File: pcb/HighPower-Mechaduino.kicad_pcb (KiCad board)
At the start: 2 copper layers, 60 x 60 mm, 124 parts, among them J1 SUPPLY, J2 STEPPER, P1 SWD, P2 USB, P3 PoStep25-32, P4 -, P5 -, P6 -, P7 -, Q1 SSM3J328R, Q10 IPD220N06L3, Q11 BSS138, Q2 BSS138, Q3 IPD220N06L3, Q4 IPD220N06L3, Q5 IPD220N06L3, Q6 IPD220N06L3, Q7 IPD220N06L3, Q8 IPD220N06L3, Q9 IPD220N06L3, SW1 SW_PUSH, U1 AS5047D, U2 AP2112K-3.3TRG1, U3 AT24CS64-SSHM, U4 SAMD21G18A-A, U5 A4955GLPTR-T, U6 A4955GLPTR-T, U7 USBLC6-2SC6, U8 MCP16331T, Y1 32.768kHz

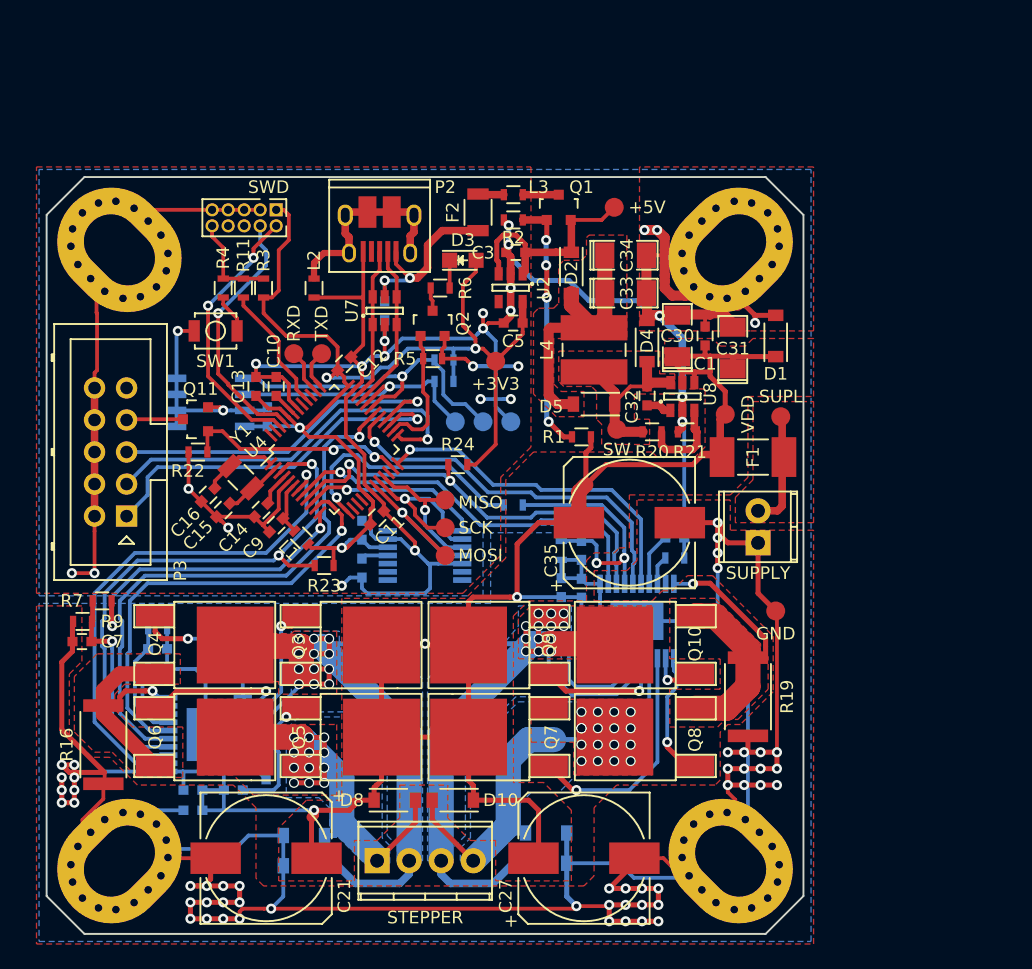
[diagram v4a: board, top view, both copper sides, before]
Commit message: Improve layout and add voltage sensing circuit to layout
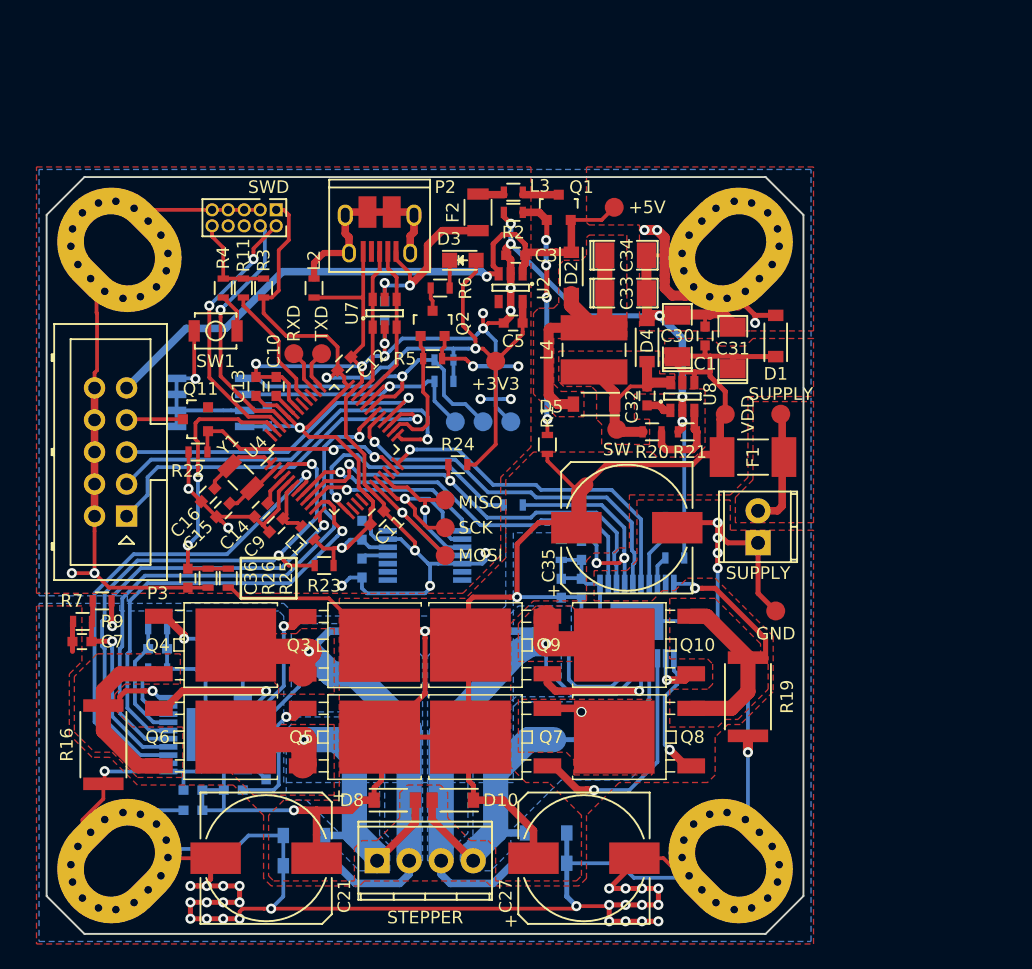
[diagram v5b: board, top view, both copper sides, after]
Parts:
- removed REF***: KiCad-Logo2_8mm_SilkScreen, Symbols:KiCad-Logo2_8mm_SilkScreen
- removed REF***: OSHW-Logo_11.4x12mm_SilkScreen, Symbols:OSHW-Logo_11.4x12mm_SilkScreen
- added C36: 100n, Capacitors_SMD:C_0603, F.Cu at (131.2, 101.8)
- added R25: 22k, Resistors_SMD:R_0603, F.Cu at (134.4, 101.8)
- added R26: 1k, Resistors_SMD:R_0603, F.Cu at (132.8, 101.8)
- Q10, Q3, Q4, Q5, Q6, Q7, Q8, Q9: footprint TO_SOT_Packages_SMD:TO-252-2Lead -> TO_SOT_Packages_SMD_local:PG-TO-252-3-313
- SW1: value SW_PUSH -> B3U-1000P
- W1: value SUPL -> SUPPLY
- Y1: value 32.768kHz -> G83270022
- moved Q10 3.35 mm to (168.1, 107.1)
- moved Q4 3.35 mm to (131.9, 107.1)
- moved Q6 3.35 mm to (131.9, 114.4)
- moved Q8 3.35 mm to (168.1, 114.4)
- moved Q3 3.15 mm to (143.3, 107.1)
- moved Q5 3.15 mm to (143.3, 114.4)
- moved Q7 3.15 mm to (156.7, 114.4)
- moved Q9 3.15 mm to (156.7, 107.1)
- moved R1 2.77 mm to (159.7, 91.2), turned to 270 degrees
- moved D12 1.00 mm to (153.4, 106.0)
- moved D6 1.00 mm to (146.6, 106.0)
- moved L1 0.64 mm to (140.7, 98.2)
- moved R2 0.60 mm to (157.0, 72.8)
- moved C35 0.45 mm to (166.0, 97.8)
- moved C3 0.23 mm to (157.2, 76.2)
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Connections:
- P3 pad 9: Net-(P3-Pad9) -> +5V
- U4 pad 47: /Arduino_Zero_Base/Arduino_A5 -> /A_IN
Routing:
- net GND: track 548.4 -> 505.9 mm, vias 78 -> 61
- net +5V: track 18.1 -> 51.8 mm, vias 0 -> 1
- net /A_IN: track 0.00 -> 22.0 mm, vias 0 -> 2
- net VDD: track 150.7 -> 166.7 mm
- net /PWM_Bridge_A4955-B/OUT2: track 51.7 -> 38.3 mm, vias 17 -> 1
- net /PWM_Bridge_A4955-A/OUT1: track 46.1 -> 34.5 mm, vias 12 -> 1
- net /PWM_Bridge_A4955-B/OUT1: track 70.1 -> 59.1 mm, vias 13 -> 1
- net /PWM_Bridge_A4955-A/OUT2: track 61.3 -> 54.8 mm, vias 12 -> 1
- net /Protected_USB_Supply/VBUS: track 0.00 -> 2.85 mm
- net Net-(F2-Pad1): track 4.92 -> 2.07 mm
- net /AIOUT1: track 41.4 -> 39.6 mm
- net Net-(Q10-Pad3): track 25.4 -> 23.8 mm
- net Net-(Q4-Pad3): track 18.4 -> 19.8 mm
- net /STP_STEP: track 28.0 -> 26.9 mm
- net Net-(Q1-Pad1): track 20.4 -> 19.3 mm
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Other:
- rule trace_min: 0.2 -> 0.3

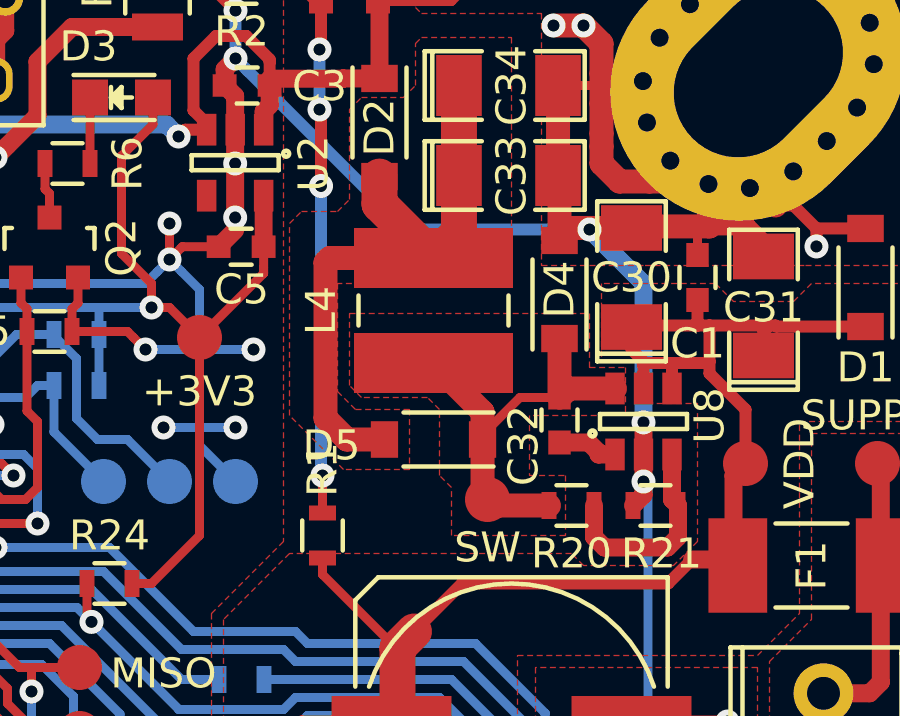
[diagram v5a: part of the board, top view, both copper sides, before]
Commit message: Fix inductor (old one was no longer available)
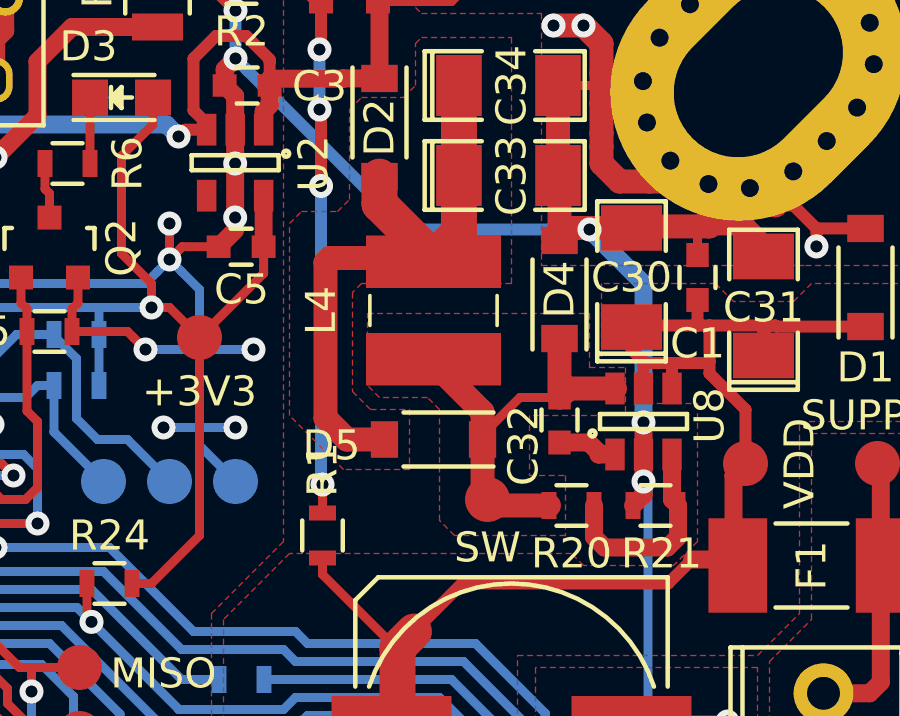
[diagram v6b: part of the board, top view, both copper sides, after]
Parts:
- L4: footprint Inductors_local:Inductor_Würth_SPC_4818 -> Inductors_local:Inductor_Würth_WE-PD2_4532
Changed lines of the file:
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@@
     (add_net /PWM_Bridge_A4955-B/OUT2)
   )
+  (module Inductors_local:Inductor_Würth_WE-PD2_4532 (layer F.Cu)
+    (at 163.4 83.7 90)
+    (descr "WE-PD2 SMD Power Inductor")
+    (tags "inductor würth")
+    (zone_connect 2)
+    (attr smd)
+    (fp_text reference L4 (at 0 -3.75 90) (layer F.SilkS)
+      (effects (font (size 1 1) (thickness 0.15)))
+    )
+    (fp_text value 22µ (at 0 0 180) (layer F.Fab)
+      (effects (font (size 1 1) (thickness 0.15)))
+    )
+    (fp_circle (center -1.8 0) (end -1.6 0) (layer F.Fab) (width 0.1))
+    (fp_arc (start 0 0) (end -1 2) (angle 126.8) (layer F.Fab) (width 0.1))
+    (fp_arc (start 0 0) (end 1 -2) (angle 126.8) (layer F.Fab) (width 0.1))
+    (fp_line (start -3 2.9) (end -3 -2.9) (layer F.CrtYd) (width 0.05))
+    (fp_line (start 3 2.9) (end -3 2.9) (layer F.CrtYd) (width 0.05))
+    (fp_line (start 3 -2.9) (end 3 2.9) (layer F.CrtYd) (width 0.05))
+    (fp_line (start -3 -2.9) (end 3 -2.9) (layer F.CrtYd) (width 0.05))
+    (fp_line (start -0.5 2.12) (end 0.5 2.12) (layer F.SilkS) (width 0.12))
+    (fp_line (start -0.5 -2.12) (end 0.5 -2.12) (layer F.SilkS) (width 0.12))
+    (fp_line (start 1 2) (end -1 2) (layer F.Fab) (width 0.1))
+    (fp_line (start -1 -2) (end 1 -2) (layer F.Fab) (width 0.1))
+    (pad 2 smd rect (at 1.625 0 90) (size 1.75 4.5) (layers F.Cu F.Paste F.Mask)
+      (net 22 /MCP16331_5V/VOUT) (zone_connect 2))
+    (pad 1 smd rect (at -1.625 0 90) (size 1.75 4.5) (layers F.Cu F.Paste F.Mask)
+      (net 21 "Net-(C32-Pad2)") (zone_connect 2))
+  )
   (module Measurement_Points:Measurement_Point_Round-SMD-Pad_Small (layer F.Cu)
     (at 177.8 104.4 180)
@@
       (effects (font (size 1 1) (thickness 0.15)))
     )
-    (fp_text value AP2112K-3.3TRG1 (at -0.05 1.988278 450) (layer F.Fab)
+    (fp_text value AP2112K-3.3TRG1 (at -0.05 1.988278 90) (layer F.Fab)
       (effects (font (size 1 1) (thickness 0.15)))
     )
@@
     )
   )
-  (module Inductors_local:Inductor_Würth_SPC_4818 (layer F.Cu)
-    (at 163.4 83.7 90)
-    (descr "WE-SPC SMD Shielded Power Inductor")
-    (tags "inductor würth")
-    (attr smd)
-    (fp_text reference L4 (at 0 -3.75 90) (layer F.SilkS)
-      (effects (font (size 1 1) (thickness 0.15)))
-    )
-    (fp_text value 22µ (at 0.1 0 180) (layer F.Fab)
-      (effects (font (size 1 1) (thickness 0.15)))
-    )
-    (fp_line (start -3 2.9) (end -3 -2.9) (layer F.CrtYd) (width 0.05))
-    (fp_line (start 3 2.9) (end -3 2.9) (layer F.CrtYd) (width 0.05))
-    (fp_line (start 3 -2.9) (end 3 2.9) (layer F.CrtYd) (width 0.05))
-    (fp_line (start -3 -2.9) (end 3 -2.9) (layer F.CrtYd) (width 0.05))
-    (fp_line (start -0.5 2.5) (end 0.5 2.5) (layer F.SilkS) (width 0.15))
-    (fp_line (start -0.5 -2.5) (end 0.5 -2.5) (layer F.SilkS) (width 0.15))
-    (fp_line (start -2.4 2.4) (end -2.4 -2.4) (layer F.Fab) (width 0.1))
-    (fp_line (start 2.4 2.4) (end -2.4 2.4) (layer F.Fab) (width 0.1))
-    (fp_line (start 2.4 -2.4) (end 2.4 2.4) (layer F.Fab) (width 0.1))
-    (fp_line (start -2.4 -2.4) (end 2.4 -2.4) (layer F.Fab) (width 0.1))
-    (pad 1 smd rect (at -1.75 0 90) (size 2 5.3) (layers F.Cu F.Paste F.Mask)
-      (net 21 "Net-(C32-Pad2)"))
-    (pad 2 smd rect (at 1.75 0 90) (size 2 5.3) (layers F.Cu F.Paste F.Mask)
-      (net 22 /MCP16331_5V/VOUT))
-  )
   (module Pin_Headers:Pin_Header_Straight_2x05_Pitch1.27mm (layer F.Cu)
     (at 138.2 72.6 270)
@@
     (tags "dpak TO-252 PG-TO-252")
     (attr smd)
-    (fp_text reference Q3 (at 0 3.35 360) (layer F.SilkS)
+    (fp_text reference Q3 (at 0 3.35) (layer F.SilkS)
       (effects (font (size 1 1) (thickness 0.15)))
     )
-    (fp_text value IPD220N06L3 (at 0.08 -1.05 360) (layer F.Fab)
+    (fp_text value IPD220N06L3 (at 0.08 -1.05) (layer F.Fab)
       (effects (font (size 1 1) (thickness 0.15)))
     )
@@
     (tags "dpak TO-252 PG-TO-252")
     (attr smd)
-    (fp_text reference Q4 (at 0 3.15 360) (layer F.SilkS)
+    (fp_text reference Q4 (at 0 3.15) (layer F.SilkS)
       (effects (font (size 1 1) (thickness 0.15)))
     )
-    (fp_text value IPD220N06L3 (at 0.1 -1.05 360) (layer F.Fab)
+    (fp_text value IPD220N06L3 (at 0.1 -1.05) (layer F.Fab)
       (effects (font (size 1 1) (thickness 0.15)))
     )
@@
     (tags "dpak TO-252 PG-TO-252")
     (attr smd)
-    (fp_text reference Q5 (at 0 3.15 360) (layer F.SilkS)
+    (fp_text reference Q5 (at 0 3.15) (layer F.SilkS)
       (effects (font (size 1 1) (thickness 0.15)))
     )
-    (fp_text value IPD220N06L3 (at 0 -1.05 540) (layer F.Fab)
+    (fp_text value IPD220N06L3 (at 0 -1.05 180) (layer F.Fab)
       (effects (font (size 1 1) (thickness 0.15)))
     )
@@
     (tags "dpak TO-252 PG-TO-252")
     (attr smd)
-    (fp_text reference Q6 (at 0 3.15 360) (layer F.SilkS)
+    (fp_text reference Q6 (at 0 3.15) (layer F.SilkS)
       (effects (font (size 1 1) (thickness 0.15)))
     )
-    (fp_text value IPD220N06L3 (at 0 -1.05 360) (layer F.Fab)
+    (fp_text value IPD220N06L3 (at 0 -1.05) (layer F.Fab)
       (effects (font (size 1 1) (thickness 0.15)))
     )
@@
   (segment (start 145.85 86.075127) (end 145.168807 86.75632) (width 0.3) (layer F.Cu) (net 36))
   (segment (start 145.168807 86.75632) (end 144.638478 87.286649) (width 0.3) (layer F.Cu) (net 36))
-  (segment (start 159.7 90.45) (end 159.7 89.2) (width 0.3) (layer F.Cu) (net 38))
-  (via (at 159.7 89.2) (size 0.8) (drill 0.4) (layers F.Cu B.Cu) (net 38))
-  (segment (start 159.65 79.55) (end 159.65 89.15) (width 0.4) (layer B.Cu) (net 38))
-  (segment (start 159.65 89.15) (end 159.7 89.2) (width 0.4) (layer B.Cu) (net 38))
+  (segment (start 159.65 89.45) (end 159.7 89.5) (width 0.4) (layer B.Cu) (net 38))
+  (segment (start 159.65 79.55) (end 159.65 89.45) (width 0.4) (layer B.Cu) (net 38))
+  (segment (start 159.7 90.45) (end 159.7 89.5) (width 0.3) (layer F.Cu) (net 38))
+  (via (at 159.7 89.5) (size 0.8) (drill 0.4) (layers F.Cu B.Cu) (net 38))
   (segment (start 157.75 72.8) (end 159.04924 72.8) (width 0.6) (layer F.Cu) (net 38))
   (segment (start 159.04924 72.8) (end 159.65 73.40076) (width 0.6) (layer F.Cu) (net 38))
@@
     (polygon
       (pts
-        (xy 163 74.6) (xy 166 74.6) (xy 166 82.8) (xy 161 82.8) (xy 160.2 82.8)
-        (xy 160.2 86.4) (xy 160.8 87) (xy 162.6 87) (xy 162.6 89) (xy 160.4 89)
+        (xy 163 74.6) (xy 166 74.6) (xy 166 82.8) (xy 161 82.8) (xy 160.7 83.1)
+        (xy 160.7 86.4) (xy 161.3 87) (xy 162.6 87) (xy 162.6 89) (xy 160.4 89)
         (xy 158.6 87.2) (xy 158.6 80.8) (xy 159 80.4) (xy 160.2 80.4) (xy 160.6 80)
         (xy 160.6 77) (xy 161 76.6) (xy 162.4 76.6) (xy 162.8 76.2) (xy 162.8 74.8)
@@
     (polygon
       (pts
-        (xy 160.6 83.8) (xy 168.6 83.8) (xy 168.6 85.6) (xy 169.8 85.6) (xy 169.8 87.2)
-        (xy 166.6 87.2) (xy 166.6 89.2) (xy 167.8 89.2) (xy 167.8 91.2) (xy 164 91.2)
-        (xy 164 89.6) (xy 163.6 89.2) (xy 163.6 87) (xy 163.2 86.6) (xy 161 86.6)
-        (xy 160.6 86.2)
+        (xy 161.2 83.8) (xy 168.6 83.8) (xy 168.6 85.6) (xy 169.8 85.6) (xy 169.8 87.2)
+        (xy 166.6 87.2) (xy 166.6 89.2) (xy 167.8 89.2) (xy 167.8 91.2) (xy 164.1 91.2)
+        (xy 163.6 90.7) (xy 163.6 87) (xy 163.2 86.6) (xy 161.6 86.6) (xy 161.2 86.2)
       )
     )

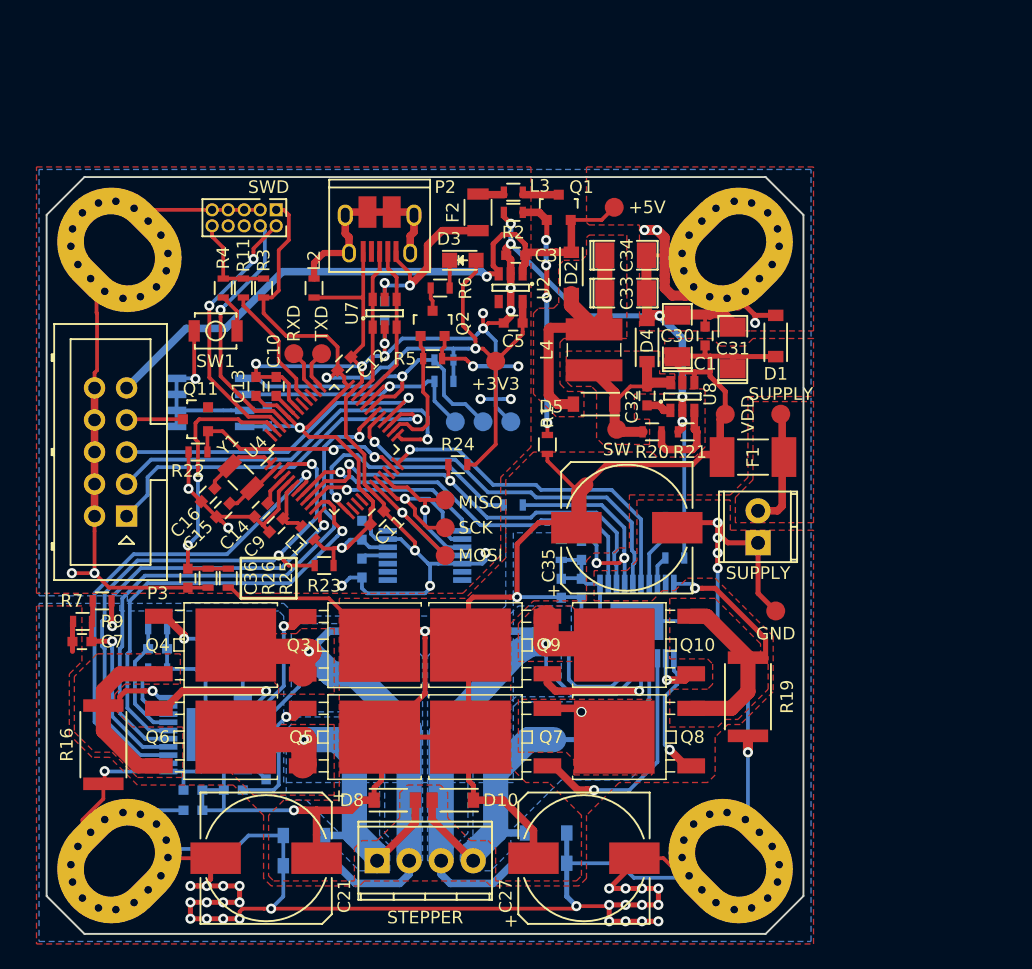
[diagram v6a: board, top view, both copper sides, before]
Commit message: Add Fiducials to pcb
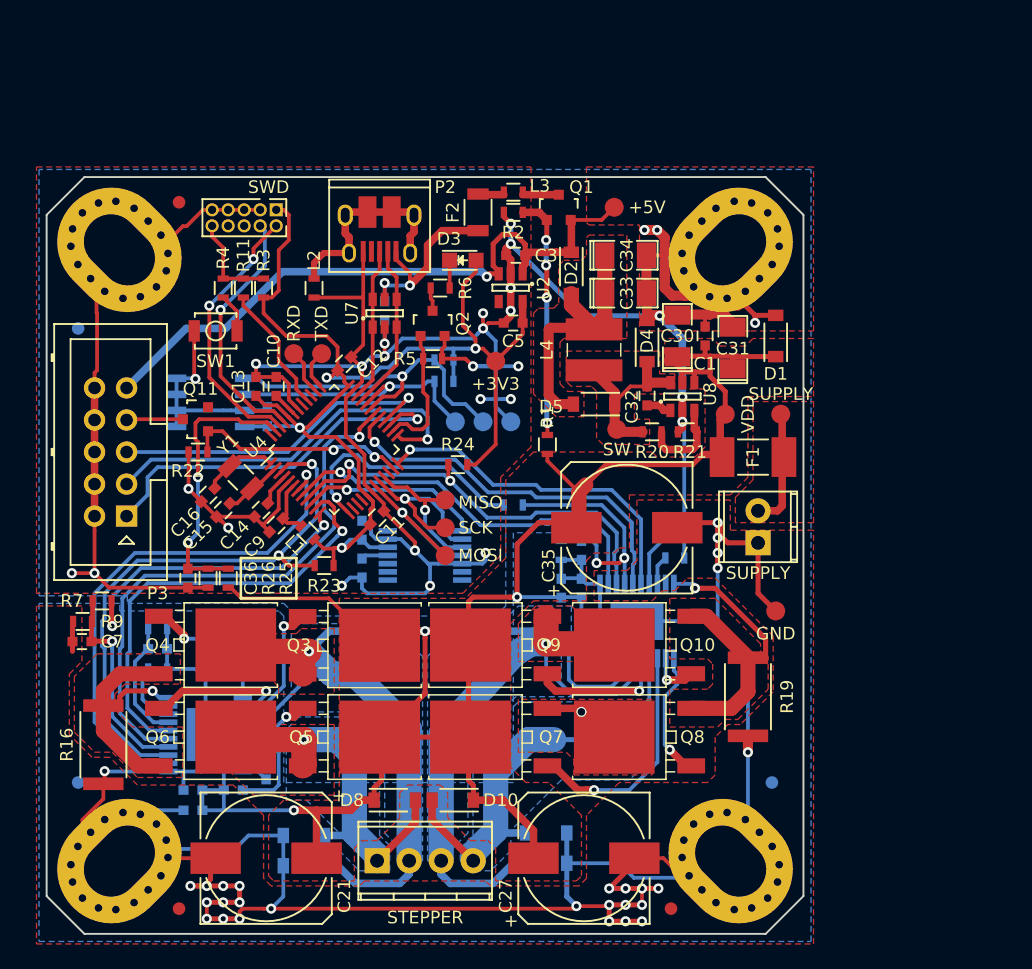
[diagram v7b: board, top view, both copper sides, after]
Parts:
- added REF**: Fiducial_1mm_Dia_2.54mm_Outer_CopperTop, Fiducials:Fiducial_1mm_Dia_2.54mm_Outer_CopperTop, F.Cu at (130.5, 72.0)
- added REF**: Fiducial_1mm_Dia_2.54mm_Outer_CopperTop, Fiducials:Fiducial_1mm_Dia_2.54mm_Outer_CopperTop, F.Cu at (169.5, 128.0)
- added REF**: Fiducial_1mm_Dia_2.54mm_Outer_CopperTop, Fiducials:Fiducial_1mm_Dia_2.54mm_Outer_CopperTop, F.Cu at (130.5, 128.0)
- added REF**: Fiducial_1mm_Dia_2.54mm_Outer_CopperTop, Fiducials:Fiducial_1mm_Dia_2.54mm_Outer_CopperTop, B.Cu at (122.5, 118.0)
- added REF**: Fiducial_1mm_Dia_2.54mm_Outer_CopperTop, Fiducials:Fiducial_1mm_Dia_2.54mm_Outer_CopperTop, B.Cu at (177.5, 118.0)
- added REF**: Fiducial_1mm_Dia_2.54mm_Outer_CopperTop, Fiducials:Fiducial_1mm_Dia_2.54mm_Outer_CopperTop, B.Cu at (122.5, 82.0)
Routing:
- net GND: track 505.9 -> 501.1 mm, vias 61 -> 57
- net /AIOUT1: track 39.6 -> 41.5 mm

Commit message: Add some improvements, fix issue with schematic error
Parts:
- added C37: 100n, Capacitors_SMD:C_0603, F.Cu at (145.4, 101.8)
- added U9: LM75BD, Housings_SOIC:SOIC-8_3.9x4.9mm_Pitch1.27mm, F.Cu at (150.0, 100.6)
- L1, L2, L3: value Ferrite_Bead -> MH1608-471Y
- Q10, Q3, Q4, Q5, Q6, Q7, Q8, Q9: value IPD220N06L3 -> IPD079N06L3G
- moved W16 3.88 mm to (153.7, 96.7)
- moved W17 3.76 mm to (153.7, 94.7)
- moved W15 3.70 mm to (153.7, 92.5)
- moved R24 2.57 mm to (153.8, 90.5)
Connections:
- net /MCP16331_5V/VOUT renamed Net-(C33-Pad1)
- net Net-(R20-Pad1) renamed /MCP16331_5V/Vfb
- R20 pad 2: Net-(C32-Pad2) -> +5V
- U3 pad 4: GND -> Net-(U3-Pad4)
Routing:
- net +5V: track 51.8 -> 74.5 mm, vias 1 -> 3
- net /SDA: track 27.5 -> 42.9 mm, vias 1 -> 2
- net /SCL: track 21.8 -> 36.2 mm, vias 1 -> 2
- net +3V3: track 99.6 -> 104.5 mm, vias 4 -> 5
- net /SPI_MISO: track 11.7 -> 15.6 mm
- net /SPI_SCK: track 13.7 -> 16.4 mm
- net Net-(C32-Pad2): track 14.5 -> 12.0 mm
- net /OCLn2: track 34.6 -> 37.0 mm
- net /SPI_MOSI: track 14.0 -> 15.5 mm
- net GND: track 501.1 -> 500.4 mm, vias 57 -> 55
- net Net-(Q1-Pad1): track 19.3 -> 19.8 mm
